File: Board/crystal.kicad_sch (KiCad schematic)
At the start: 4 parts, among them Y1 Crystal_GND24

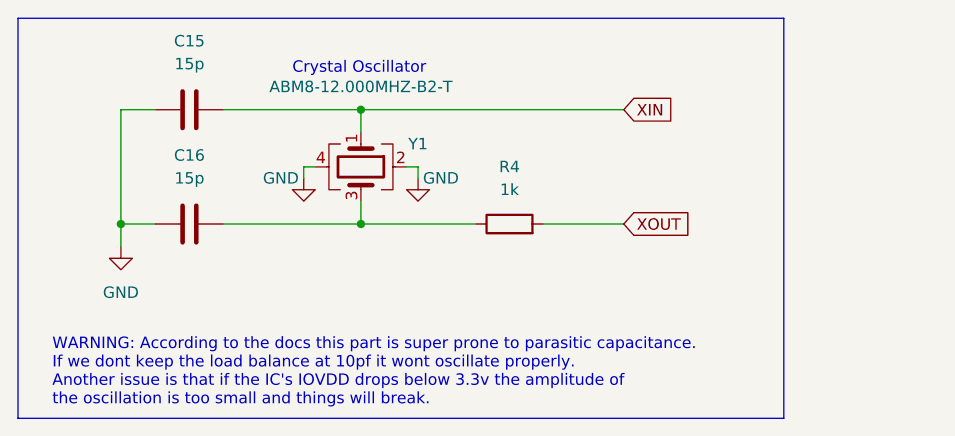
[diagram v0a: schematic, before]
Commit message: Touch-up module schematics
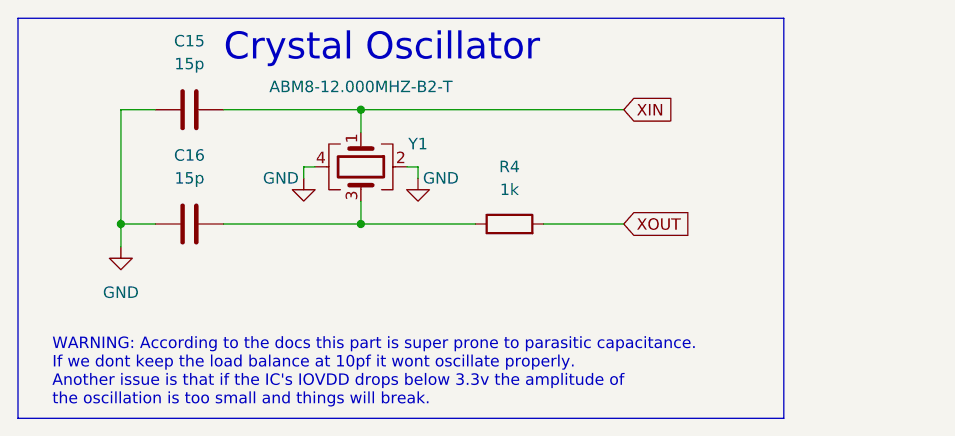
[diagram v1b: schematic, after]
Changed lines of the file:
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@@
     (effects (font (size 1.27 1.27)) (justify left bottom))
   )
-  (text "Crystal Oscillator\n" (at 140.97 63.5 0)
-    (effects (font (size 1.27 1.27)) (justify left bottom))
+  (text "Crystal Oscillator\n" (at 133.35 62.23 0)
+    (effects (font (size 3 3)) (justify left bottom))
   )
   (global_label "XIN" (shape input) (at 177.8 67.31 0) (fields_autoplaced)
